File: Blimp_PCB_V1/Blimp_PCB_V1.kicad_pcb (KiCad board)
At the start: 2 copper layers, 109.9 x 62 mm, 29 parts, among them J1 S8B-PH-K-S

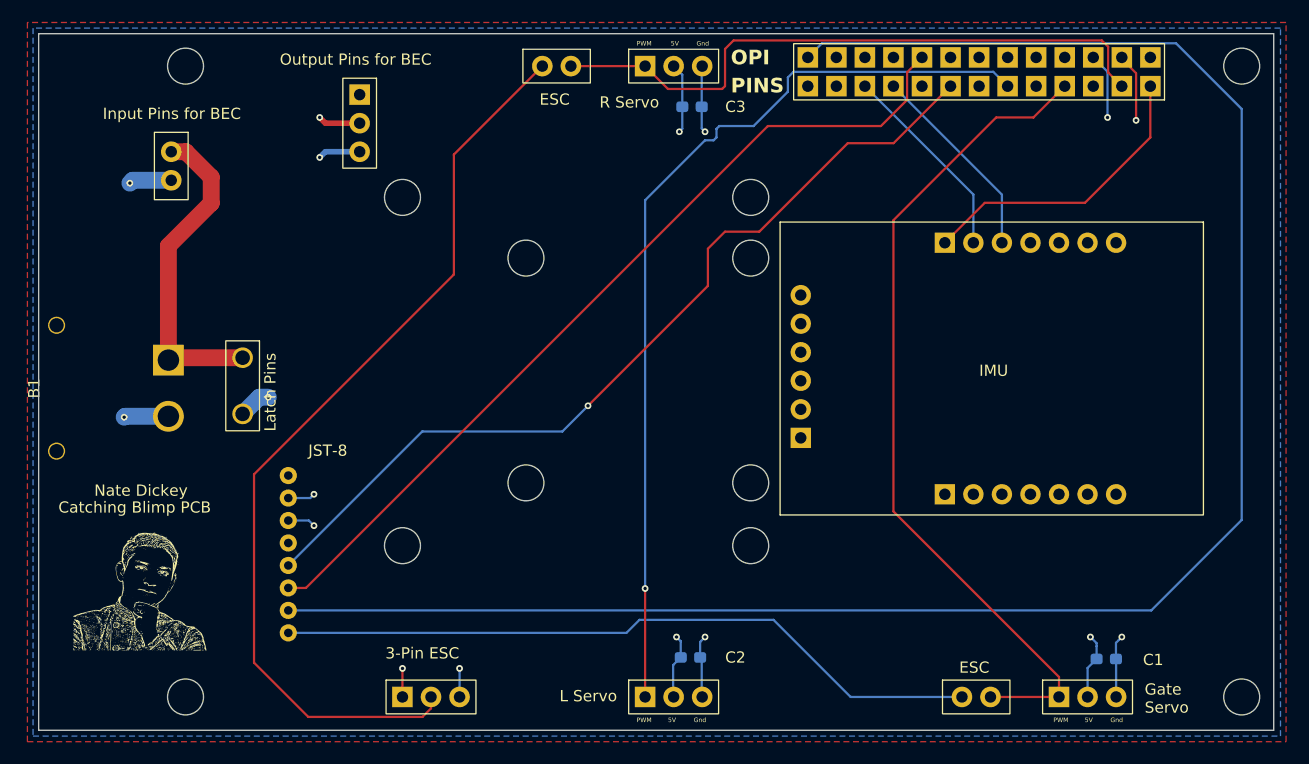
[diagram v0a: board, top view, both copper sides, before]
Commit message: PCBv1 modified schematic
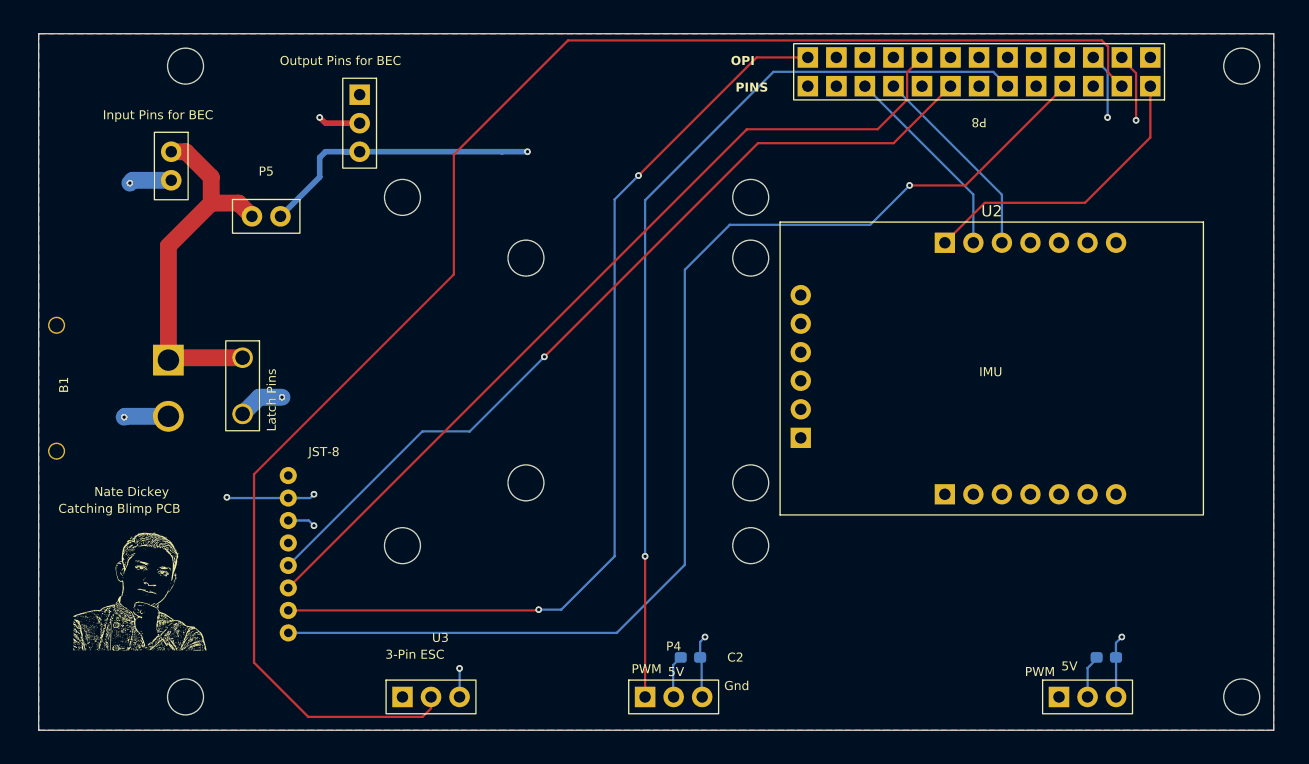
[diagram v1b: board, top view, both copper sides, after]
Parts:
- removed C1: 100uF, Capacitor_SMD:C_0603_1608Metric_Pad1.08x0.95mm_HandSolder
- removed P6, P7: ~, PINS:Shorting Pins
- P4, U3: footprint PINS:PWM -> Pins:PWM
- P5: footprint PINS:PWM -> Pins:Shorting Pins
- P8: footprint PINS:26-PIN Female -> Blimp Library:Orange_Pi_5B
- moved C3 61.3 mm to (197.5, 124.5)
- moved P5 38.6 mm to (122.8, 85.2)
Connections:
- J1 pad 5: Net-(J1-Pad5) -> Net-(P8-CAN2_RX)
- J1 pad 7: Net-(J1-Pad7) -> Net-(P8-PWM1)
- J1 pad 8: Net-(J1-Pad8) -> Net-(P8-PWM15)
- P2 pad 1: Net-(P2-PWM) -> unconnected-(P2-PWM-Pad1)
- P5 pad 1: Net-(P5-PWM) -> BV
- P5 pad 2: +5V -> GND
- P8 pad 10: Net-(P8-Pad10) -> unconnected-(P8-TXD.0-Pad10)
- P8 pad 11: Net-(P8-Pad11) -> Net-(P4-PWM)
- P8 pad 14: Net-(J1-Pad7) -> unconnected-(P8-GND-Pad14)
- P8 pad 15: unconnected-(P8-Pad15) -> Net-(P8-CAN2_RX)
- P8 pad 19: unconnected-(P8-Pad19) -> Net-(P8-SPI4_TXD)
- P8 pad 2: Net-(P5-PWM) -> unconnected-(P8-5V-Pad2)
- P8 pad 21: unconnected-(P8-Pad21) -> Net-(P8-SPI4_RXD)
- P8 pad 24: GND -> unconnected-(P8-SPI4_CS1-Pad24)
- P8 pad 25: +5V -> unconnected-(P8-GND-Pad25)
- P8 pad 26: unconnected-(P8-Pad26) -> Net-(P8-PWM1)
- P8 pad 3: unconnected-(P8-Pad3) -> Net-(P8-SDA.5)
- P8 pad 4: Net-(P2-PWM) -> +5V
- P8 pad 6: Net-(P4-PWM) -> GND
- P8 pad 7: unconnected-(P8-Pad7) -> Net-(P8-PWM15)
- P8 pad 8: Net-(J1-Pad5) -> unconnected-(P8-RXD.0-Pad8)
- U2 pad 5: Net-(P8-Pad10) -> Net-(P8-SPI4_TXD)
- U2 pad 6: Net-(P8-Pad11) -> Net-(P8-SPI4_RXD)
- U3 pad 1: +5V -> unconnected-(U3-Pad1)
- U3 pad 2: Net-(P6-Pad1) -> Net-(P8-SDA.5)
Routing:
- net Net-(J1-Pad7): track 166.3 -> 0.00 mm
- net Net-(P8-SDA.5): track 0.00 -> 138.3 mm
- net Net-(P8-PWM15): track 0.00 -> 104.6 mm, vias 0 -> 1
- net Net-(P8-PWM1): track 0.00 -> 85.2 mm, vias 0 -> 2
- net Net-(P6-Pad1): track 82.8 -> 0.00 mm
- net Net-(J1-Pad5): track 78.5 -> 0.00 mm, vias 1 -> 0
- net Net-(P8-CAN2_RX): track 0.00 -> 76.6 mm, vias 0 -> 1
- net Net-(P2-PWM): track 74.8 -> 0.00 mm
- net Net-(J1-Pad8): track 63.3 -> 0.00 mm
- net Net-(P5-PWM): track 56.6 -> 0.00 mm
- net GND: track 45.1 -> 69.8 mm
- net Net-(P8-SPI4_RXD): track 0.00 -> 17.9 mm
- net Net-(P8-Pad11): track 17.9 -> 0.00 mm
- net Net-(P8-SPI4_TXD): track 0.00 -> 17.9 mm
- net Net-(P8-Pad10): track 17.9 -> 0.00 mm
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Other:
- board text added: "GND"
- board text removed: "C1"
- board text removed: "C3"
- board text removed: "ESC"
- board text removed: "Gate Servo"
- board text removed: "L Servo"
- board text removed: "R Servo"

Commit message: Added proper JST Connector for Lidar, Footprint and Symbol
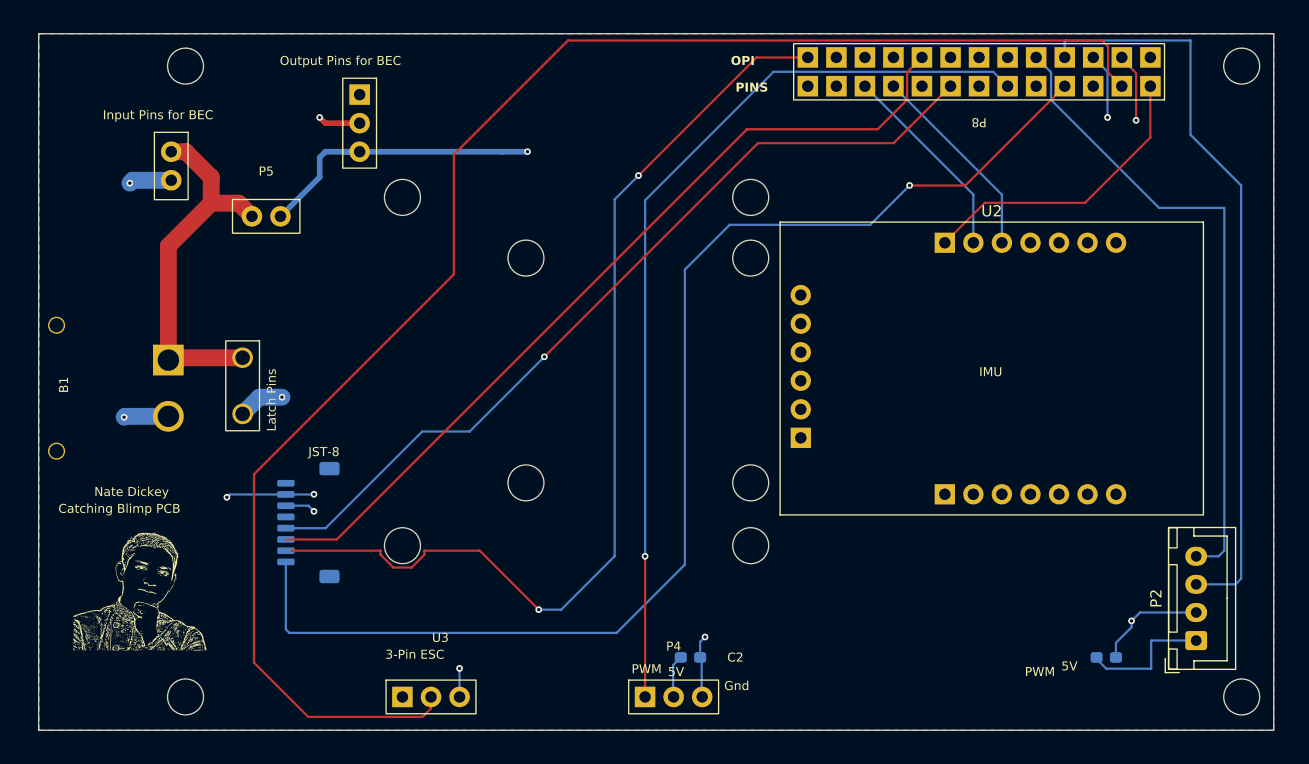
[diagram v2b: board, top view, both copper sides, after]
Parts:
- J1: footprint JST Connector:S8B-PH-K-S -> JST Connector:JST_SH_SM08B-SRSS-TB_1x08-1MP_P1.00mm_Horizontal
- P2: footprint PINS:PWM -> JST Connector:JST_XH_B4B-XH-A_1x04_P2.50mm_Vertical
- moved P2 10.9 mm to (205.5, 123.0), turned to 90 degrees
- moved J1 3.33 mm to (126.5, 112.5)
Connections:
- P2 pad 1: unconnected-(P2-PWM-Pad1) -> +5V
- P2 pad 2: +5V -> GND
- P2 pad 3: GND -> Net-(P2-L1)
- P8 pad 10: unconnected-(P8-TXD.0-Pad10) -> Net-(P2-L2)
- P8 pad 8: unconnected-(P8-RXD.0-Pad8) -> Net-(P2-L1)
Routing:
- net Net-(P2-L1): track 0.00 -> 66.6 mm
- net Net-(P2-L2): track 0.00 -> 56.9 mm
- net +5V: track 17.4 -> 25.4 mm
- net Net-(P8-PWM15): track 104.6 -> 111.0 mm
- net GND: track 69.8 -> 73.4 mm
- net Net-(P8-PWM1): track 85.2 -> 88.8 mm
- net Net-(P8-SCL.1): track 77.4 -> 75.8 mm
- net Net-(P8-CAN2_RX): track 76.6 -> 75.4 mm

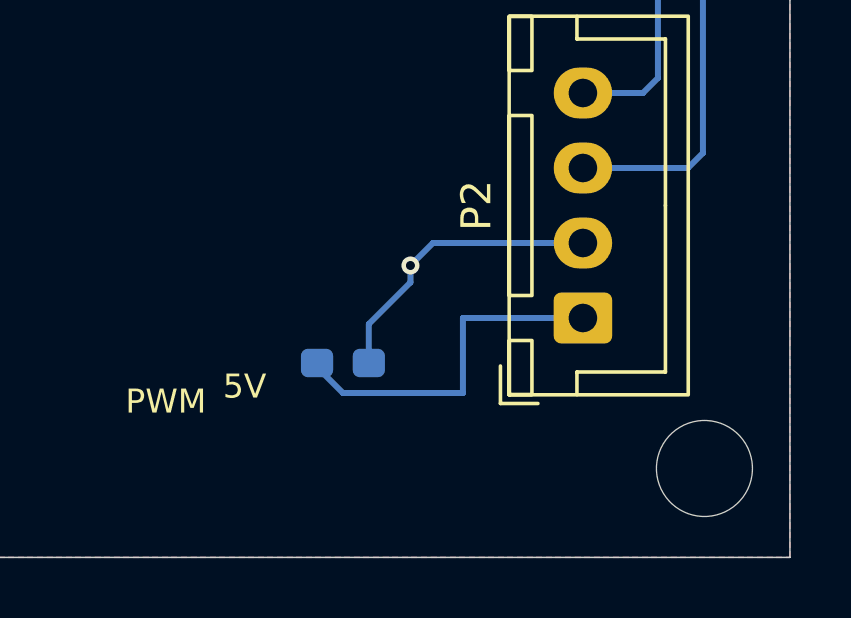
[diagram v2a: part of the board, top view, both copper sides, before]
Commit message: Tiny wiring fix
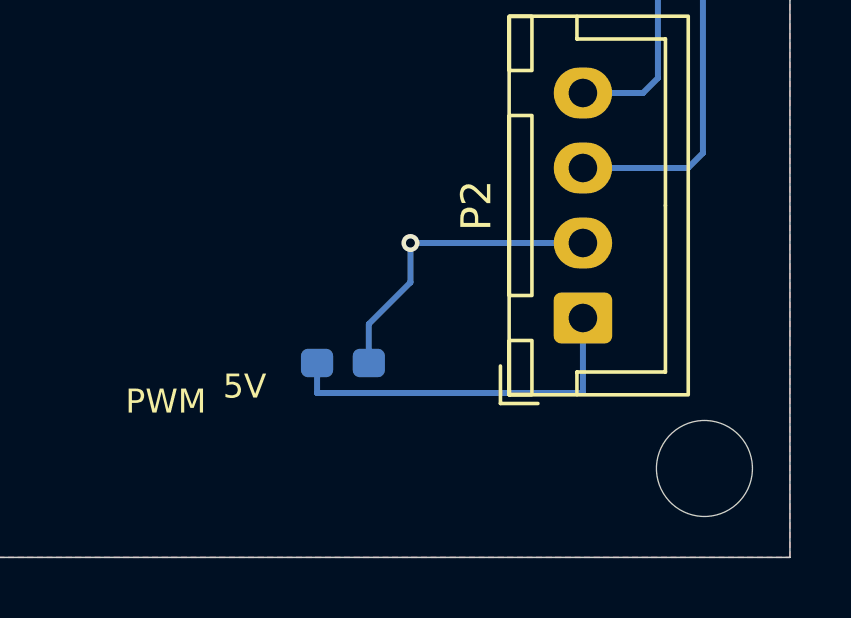
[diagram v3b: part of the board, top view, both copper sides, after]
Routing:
- net +5V: track 25.4 -> 25.9 mm
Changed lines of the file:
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@@
 	)
 	(via
-		(at 199.75 121.25)
+		(at 199.75 120.5)
 		(size 0.6)
 		(drill 0.3)
@@
 		(drill 0.3)
 		(layers "F.Cu" "B.Cu")
-		(net 1)
-	)
-	(segment
-		(start 200.5 120.5)
-		(end 205.5 120.5)
-		(width 0.2)
-		(layer "B.Cu")
 		(net 1)
 	)
@@
 	)
 	(segment
+		(start 114.046 103.044)
+		(end 110.189 103.044)
+		(width 1.5)
+		(layer "B.Cu")
+		(net 1)
+	)
+	(segment
+		(start 143.748 79.502)
+		(end 129.75 79.502)
+		(width 0.5)
+		(layer "B.Cu")
+		(net 1)
+	)
+	(segment
+		(start 127 111.5)
+		(end 126.5 111)
+		(width 0.2)
+		(layer "B.Cu")
+		(net 1)
+	)
+	(segment
+		(start 127.508 81.762)
+		(end 124.02 85.25)
+		(width 0.5)
+		(layer "B.Cu")
+		(net 1)
+	)
+	(segment
+		(start 199.75 120.5)
+		(end 199.75 121.814)
+		(width 0.2)
+		(layer "B.Cu")
+		(net 1)
+	)
+	(segment
+		(start 120.436 103.044)
+		(end 120.65 102.83)
+		(width 0.2)
+		(layer "B.Cu")
+		(net 1)
+	)
+	(segment
+		(start 124.5 110)
+		(end 119.5 110)
+		(width 0.2)
+		(layer "B.Cu")
+		(net 1)
+	)
+	(segment
+		(start 199.75 120.5)
+		(end 205.5 120.5)
+		(width 0.2)
+		(layer "B.Cu")
+		(net 1)
+	)
+	(segment
+		(start 122.134 101.346)
+		(end 120.65 102.83)
+		(width 1.5)
+		(layer "B.Cu")
+		(net 1)
+	)
+	(segment
 		(start 198.3625 123.2015)
 		(end 198.3625 124.5)
@@
 	)
 	(segment
-		(start 114.046 103.044)
-		(end 110.189 103.044)
-		(width 1.5)
-		(layer "B.Cu")
-		(net 1)
-	)
-	(segment
-		(start 143.748 79.502)
-		(end 129.75 79.502)
-		(width 0.5)
+		(start 128.016 79.502)
+		(end 127.508 80.01)
+		(width 0.5)
+		(layer "B.Cu")
+		(net 1)
+	)
+	(segment
+		(start 110.189 103.044)
+		(end 110.109 103.124)
+		(width 1.5)
+		(layer "B.Cu")
+		(net 1)
+	)
+	(segment
+		(start 161.5 124.6375)
+		(end 161.3625 124.5)
+		(width 0.2)
+		(layer "B.Cu")
+		(net 1)
+	)
+	(segment
+		(start 161.5 128)
+		(end 161.5 124.6375)
+		(width 0.2)
+		(layer "B.Cu")
+		(net 1)
+	)
+	(segment
+		(start 126.5 111)
+		(end 124.5 111)
+		(width 0.2)
 		(layer "B.Cu")
 		(net 1)
@@
 	)
 	(segment
-		(start 127 111.5)
-		(end 126.5 111)
-		(width 0.2)
-		(layer "B.Cu")
-		(net 1)
-	)
-	(segment
-		(start 127.508 81.762)
-		(end 124.02 85.25)
-		(width 0.5)
-		(layer "B.Cu")
-		(net 1)
-	)
-	(segment
-		(start 120.436 103.044)
-		(end 120.65 102.83)
-		(width 0.2)
-		(layer "B.Cu")
-		(net 1)
-	)
-	(segment
-		(start 124.5 110)
-		(end 119.5 110)
-		(width 0.2)
-		(layer "B.Cu")
-		(net 1)
-	)
-	(segment
-		(start 122.134 101.346)
-		(end 120.65 102.83)
-		(width 1.5)
-		(layer "B.Cu")
-		(net 1)
-	)
-	(segment
-		(start 199.75 121.25)
-		(end 199.75 121.814)
-		(width 0.2)
-		(layer "B.Cu")
-		(net 1)
-	)
-	(segment
-		(start 128.016 79.502)
-		(end 127.508 80.01)
-		(width 0.5)
-		(layer "B.Cu")
-		(net 1)
-	)
-	(segment
-		(start 110.189 103.044)
-		(end 110.109 103.124)
-		(width 1.5)
-		(layer "B.Cu")
-		(net 1)
-	)
-	(segment
-		(start 161.5 124.6375)
-		(end 161.3625 124.5)
-		(width 0.2)
-		(layer "B.Cu")
-		(net 1)
-	)
-	(segment
-		(start 161.5 128)
-		(end 161.5 124.6375)
-		(width 0.2)
-		(layer "B.Cu")
-		(net 1)
-	)
-	(segment
-		(start 126.5 111)
-		(end 124.5 111)
-		(width 0.2)
-		(layer "B.Cu")
-		(net 1)
-	)
-	(segment
 		(start 197.612 72.38)
 		(end 197.612 76.454)
@@
 	)
 	(segment
-		(start 199.75 121.25)
-		(end 200.5 120.5)
-		(width 0.2)
-		(layer "B.Cu")
-		(net 1)
-	)
-	(segment
 		(start 124.154 101.346)
 		(end 122.134 101.346)
@@
 	)
 	(segment
-		(start 201.5 123)
-		(end 205.5 123)
-		(width 0.2)
-		(layer "B.Cu")
-		(net 2)
-	)
-	(segment
-		(start 201.5 125.5)
-		(end 201.5 123)
-		(width 0.2)
-		(layer "B.Cu")
-		(net 2)
-	)
-	(segment
-		(start 201.5 125.5)
-		(end 197.5 125.5)
-		(width 0.2)
-		(layer "B.Cu")
-		(net 2)
-	)
-	(segment
-		(start 197.5 125.5)
+		(start 196.6375 125.5)
 		(end 196.6375 124.6375)
+		(width 0.2)
+		(layer "B.Cu")
+		(net 2)
+	)
+	(segment
+		(start 205.5 123)
+		(end 205.5 125.5)
 		(width 0.2)
 		(layer "B.Cu")
@@
 		(width 0.2)
 		(layer "B.Cu")
+		(net 2)
+	)
+	(segment
+		(start 205.5 125.5)
+		(end 196.6375 125.5)
+		(width 0.2)
+		(layer "B.Cu")

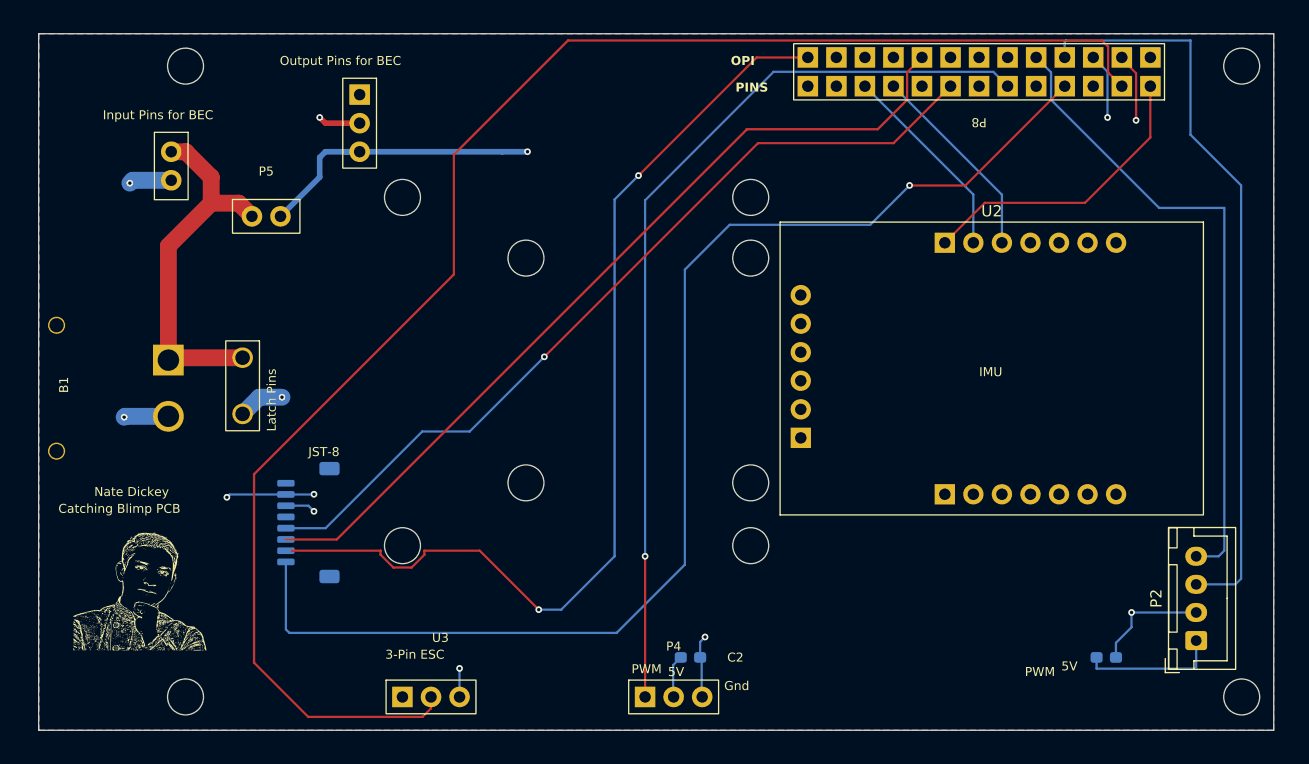
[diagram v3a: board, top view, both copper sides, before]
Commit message: Flipped lidar connection and connected 5V, confused why not connected before
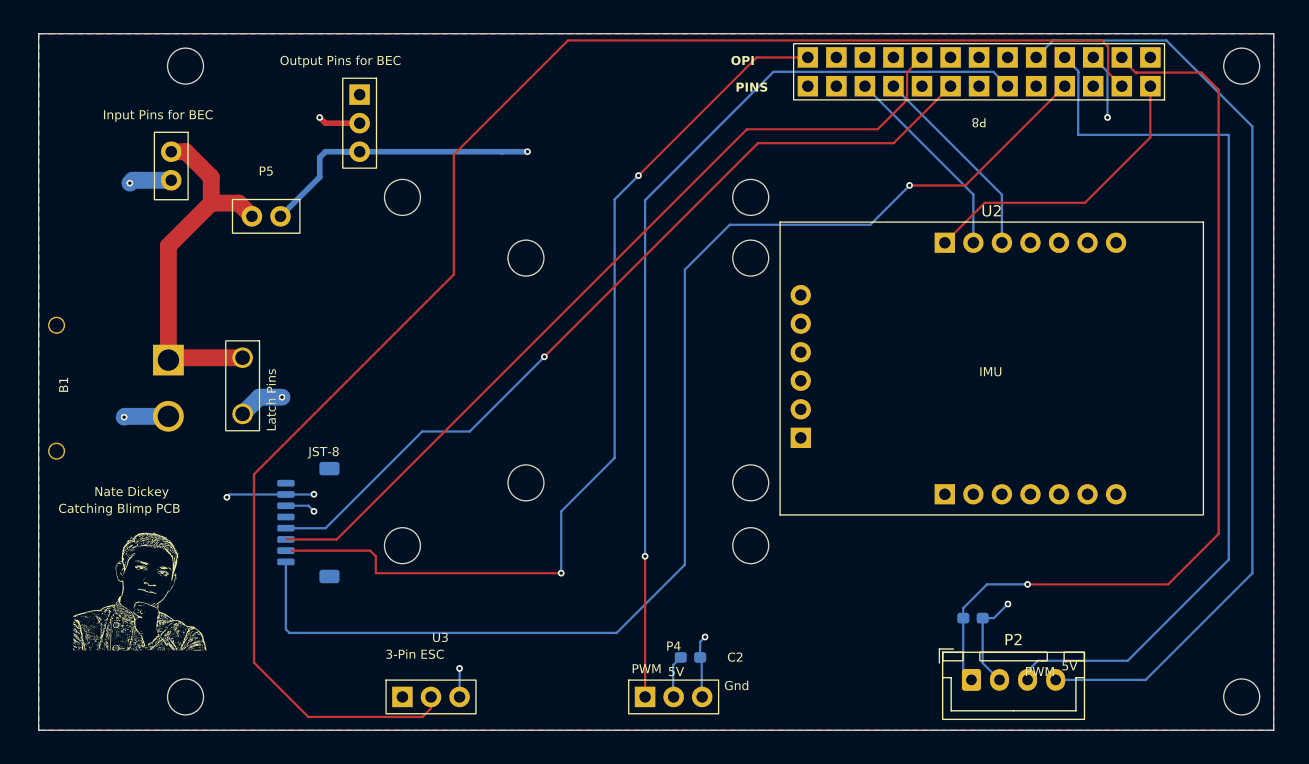
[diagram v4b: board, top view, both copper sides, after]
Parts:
- moved P2 20.3 mm to (185.5, 126.5), turned to 0 degrees
- moved C3 12.4 mm to (185.6, 121.0)
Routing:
- net +5V: track 25.9 -> 89.2 mm
- net Net-(P2-L2): track 56.9 -> 84.6 mm
- net Net-(P2-L1): track 66.6 -> 81.4 mm
- net Net-(P8-PWM1): track 88.8 -> 83.4 mm
- net GND: track 73.8 -> 72.4 mm
